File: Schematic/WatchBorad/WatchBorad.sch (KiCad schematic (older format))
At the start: 55 parts, among them IC1 TXS0108E, J1 Conn_01x06_Male, J10 Conn_01x07_Female, J2 Conn_01x09_Female, J3 USB_B_Mini, J4 Conn_01x10_Female, J5 Conn_01x06_Female, J6 Conn_01x04_Male, J7 Conn_01x11_Female, J8 Conn_01x11_Female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

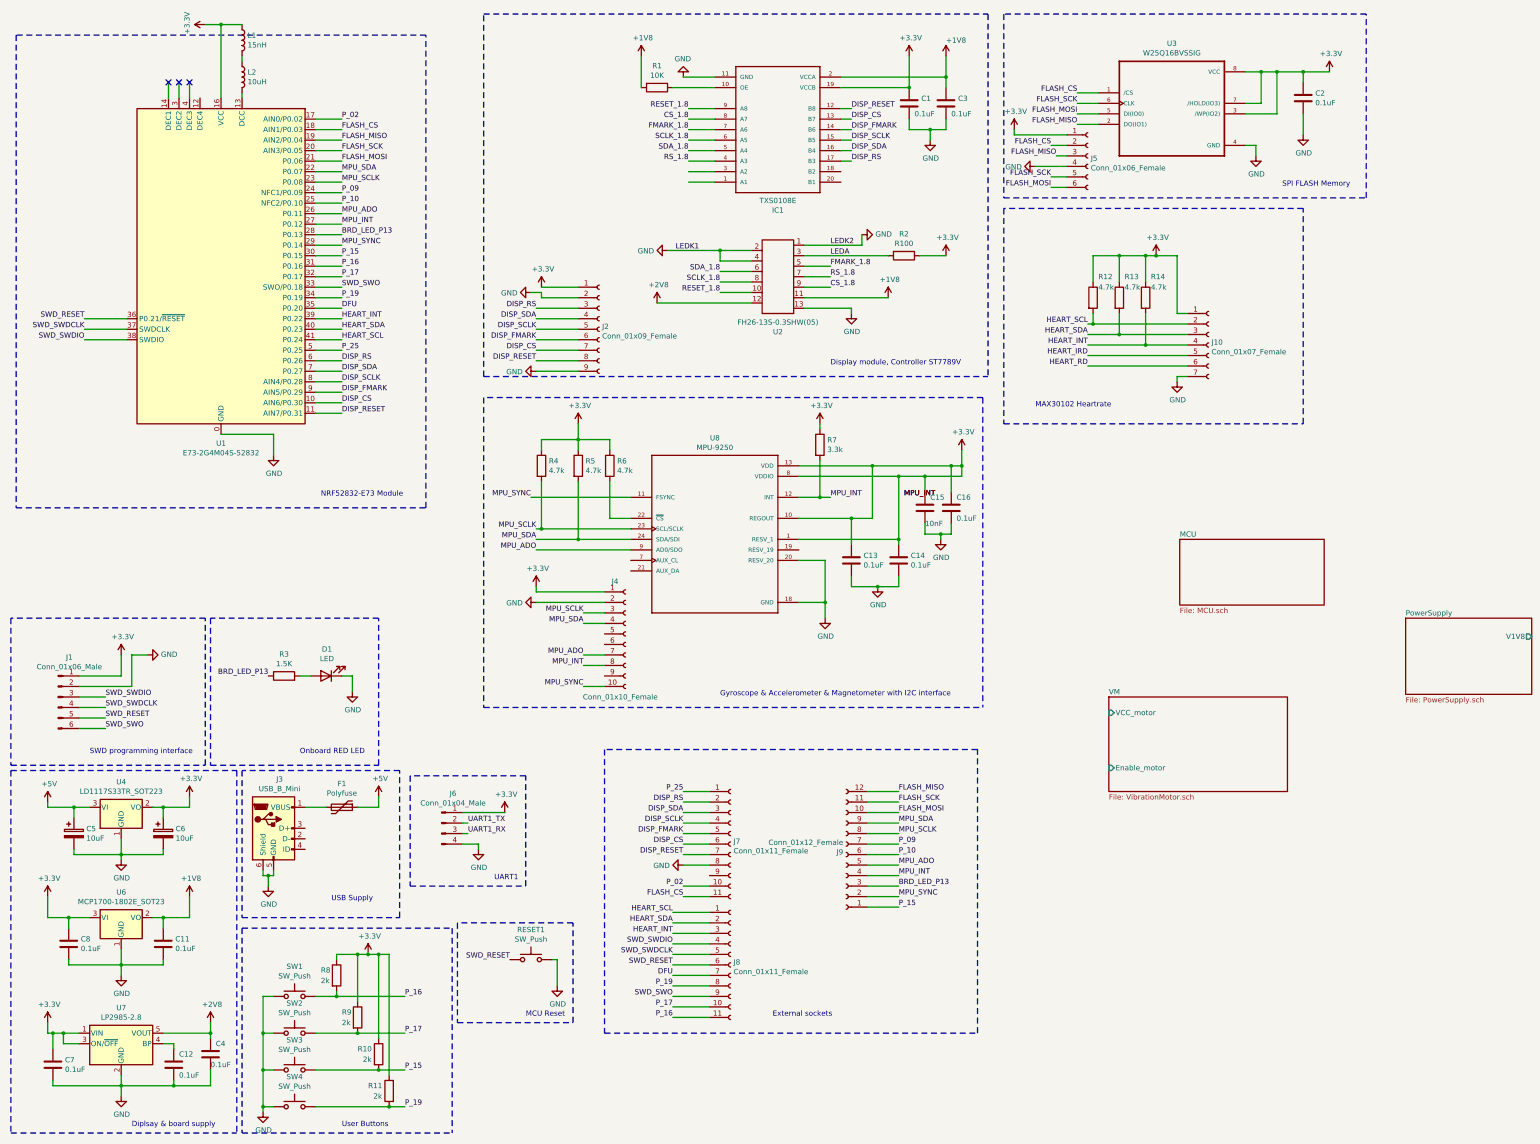
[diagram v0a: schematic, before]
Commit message: Added on/off circuit for PON and added other changes
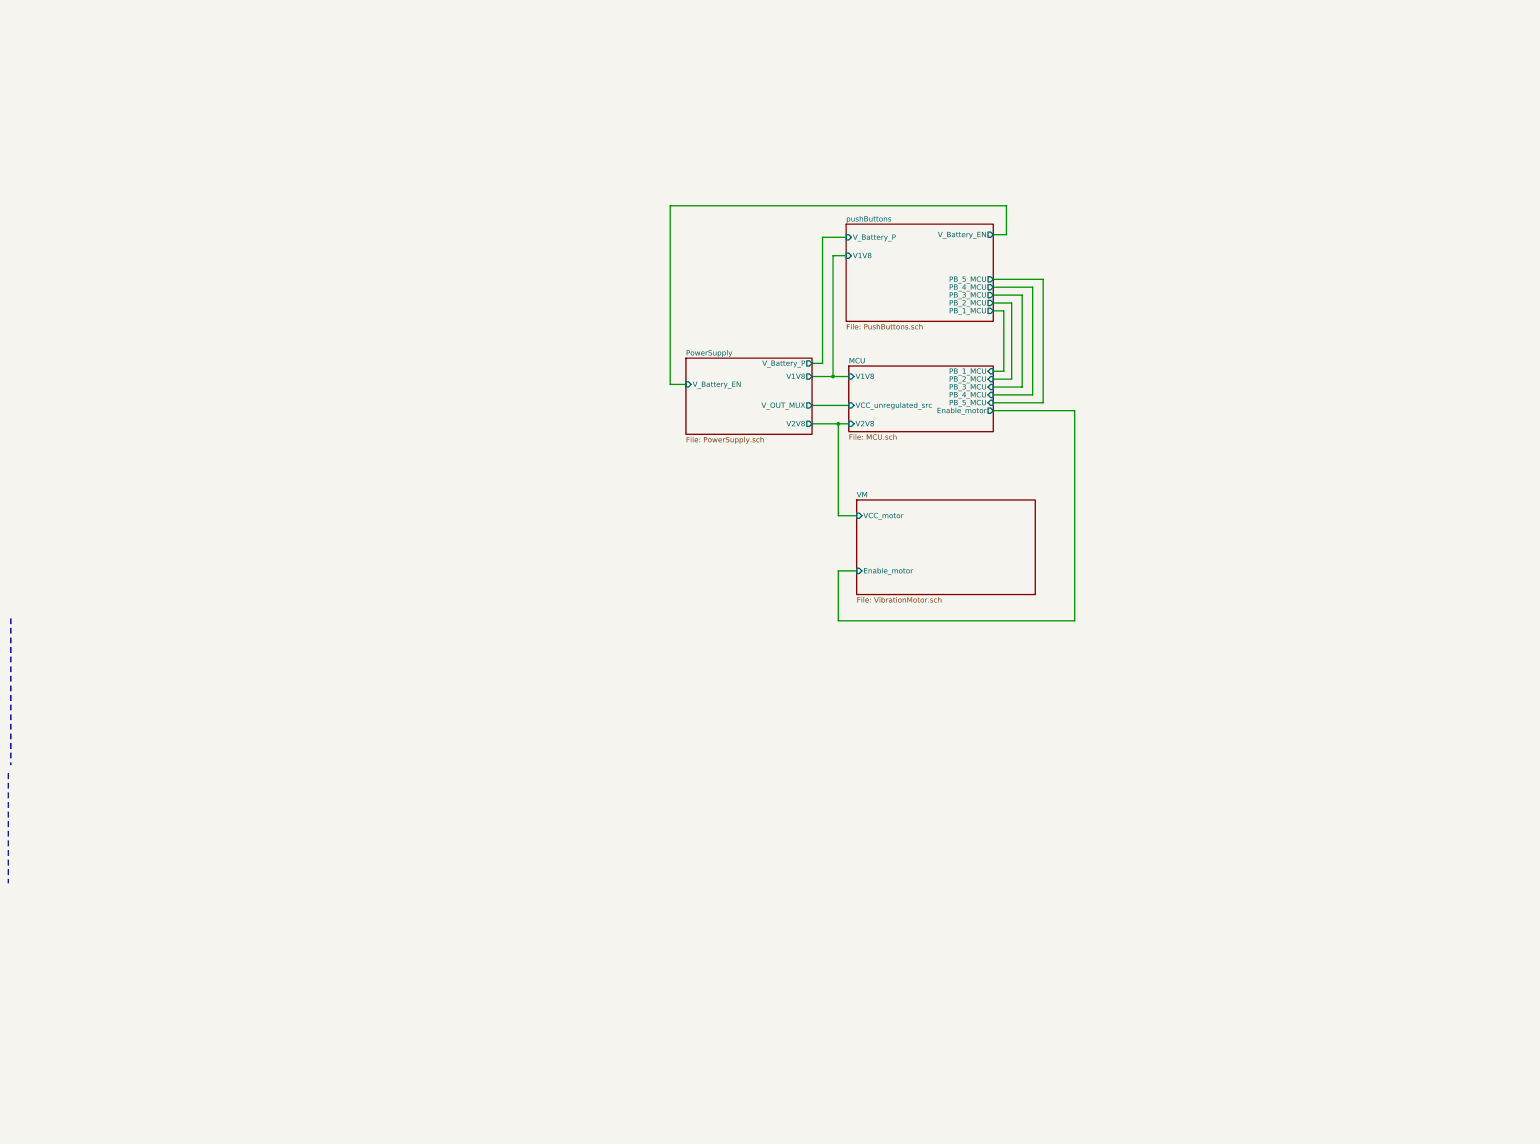
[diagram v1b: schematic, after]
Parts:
- removed C1, C11, C12, C13, C14, C16, C2, C3, C4, C7, C8: 0.1uF, Capacitor_SMD:C_0805_2012Metric_Pad1.15x1.40mm_HandSolder, symbol Device:C
- removed C15: 10nF, Capacitor_SMD:C_0805_2012Metric_Pad1.15x1.40mm_HandSolder, symbol Device:C
- removed C5, C6: 10uF, Capacitor_SMD:CP_Elec_4x3.9, symbol Device:CP
- removed D1: LED, LED_SMD:LED_0805_2012Metric_Pad1.15x1.40mm_HandSolder, symbol Device:LED
- removed F1: Polyfuse, Fuse:Fuse_1206_3216Metric_Pad1.42x1.75mm_HandSolder, symbol Device:Polyfuse
- removed IC1: TXS0108E, TXS0108E:PW_R-PDSO-G20, symbol WatchBorad-rescue:TXS0108E-TXS0108E
- removed J1: Conn_01x06_Male, Connector_PinHeader_2.54mm:PinHeader_1x06_P2.54mm_Vertical, symbol Connector:Conn_01x06_Male
- removed J10: Conn_01x07_Female, Connector_PinSocket_2.54mm:PinSocket_1x07_P2.54mm_Vertical, symbol Connector:Conn_01x07_Female
- removed J2: Conn_01x09_Female, Connector_PinSocket_2.54mm:PinSocket_1x09_P2.54mm_Vertical, symbol Connector:Conn_01x09_Female
- removed J3: USB_B_Mini, Connector_USB:USB_Mini-B_Lumberg_2486_01_Horizontal, symbol Connector:USB_B_Mini
- removed J4: Conn_01x10_Female, Connector_PinSocket_2.54mm:PinSocket_1x10_P2.54mm_Vertical, symbol Connector:Conn_01x10_Female
- removed J5: Conn_01x06_Female, Connector_PinSocket_2.54mm:PinSocket_1x06_P2.54mm_Vertical, symbol Connector:Conn_01x06_Female
- removed J6: Conn_01x04_Male, Connector_PinHeader_2.54mm:PinHeader_1x04_P2.54mm_Vertical, symbol Connector:Conn_01x04_Male
- removed J7, J8: Conn_01x11_Female, Connector_PinSocket_2.54mm:PinSocket_1x11_P2.54mm_Vertical, symbol Connector:Conn_01x11_Female
- removed J9: Conn_01x12_Female, Connector_PinSocket_2.54mm:PinSocket_1x12_P2.54mm_Vertical, symbol Connector:Conn_01x12_Female
- removed L1: 15nH, Inductor_SMD:L_0805_2012Metric_Pad1.15x1.40mm_HandSolder, symbol Device:L
- removed L2: 10uH, Inductor_SMD:L_0805_2012Metric_Pad1.15x1.40mm_HandSolder, symbol Device:L
- removed R1: 10K, Resistor_SMD:R_0805_2012Metric_Pad1.15x1.40mm_HandSolder, symbol Device:R
- removed R10, R11, R8, R9: 2k, Resistor_SMD:R_0805_2012Metric_Pad1.15x1.40mm_HandSolder, symbol Device:R
- removed R12, R13, R14: 4.7k, Resistor_SMD:R_0805_2012Metric, symbol Device:R
- removed R2: R100, Resistor_SMD:R_0805_2012Metric_Pad1.15x1.40mm_HandSolder, symbol Device:R
- removed R3: 1.5K, Resistor_SMD:R_0805_2012Metric_Pad1.15x1.40mm_HandSolder, symbol Device:R
- removed R4, R5, R6: 4.7k, Resistor_SMD:R_0805_2012Metric_Pad1.15x1.40mm_HandSolder, symbol Device:R
- removed R7: 3.3k, Resistor_SMD:R_0805_2012Metric_Pad1.15x1.40mm_HandSolder, symbol Device:R
- removed RESET1, SW1, SW2, SW3, SW4: SW_Push, Button_Switch_SMD:SW_SPST_SKQG_WithStem, symbol Switch:SW_Push
- removed U1: E73-2G4M04S-52832, RF_Module:E73-2G4M04S, symbol WatchBorad-rescue:E73-2G4M04S-52832-RF_Module
- removed U2: FH26-13S-0.3SHW(05), FH26W-13S-0:FH26-13S-0.3SHW(05), symbol WatchBorad-rescue:FH26-13S-0.3SHW(05)-Hirose_connectors
- removed U3: W25Q16BVSSIG, W25Q16BVSSIG:SOIC127P790X216-8N, symbol WatchBorad-rescue:W25Q16BVSSIG-W25Q16BVSSIG
- removed U4: LD1117S33TR_SOT223, Package_TO_SOT_SMD:SOT-223-3_TabPin2, symbol Regulator_Linear:LD1117S33TR_SOT223
- removed U6: MCP1700-1802E_SOT23, Package_TO_SOT_SMD:SOT-23, symbol Regulator_Linear:MCP1700-1802E_SOT23
- removed U7: LP2985-2.8, Package_TO_SOT_SMD:SOT-23-5, symbol Regulator_Linear:LP2985-2.8
- removed U8: MPU-9250, QFN40P300X300X105-24N, symbol WatchBorad-rescue:MPU-9250-MPU-9250
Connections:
- no-connect marks 3 -> 0
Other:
- note removed: "Diplsay & board supply"
- note removed: "Display module, Controller ST7789V"
- note removed: "External sockets"
- note removed: "Gyroscope & Accelerometer & Magnetometer with I2C interface"
- note removed: "MAX30102 Heartrate"
- note removed: "MCU Reset"
- note removed: "NRF52832-E73 Module"
- note removed: "Onboard RED LED"
- note removed: "SPI FLASH Memory\n"
- note removed: "SWD programming interface"
- note removed: "UART1"
- note removed: "USB Supply"
- note removed: "User Buttons"

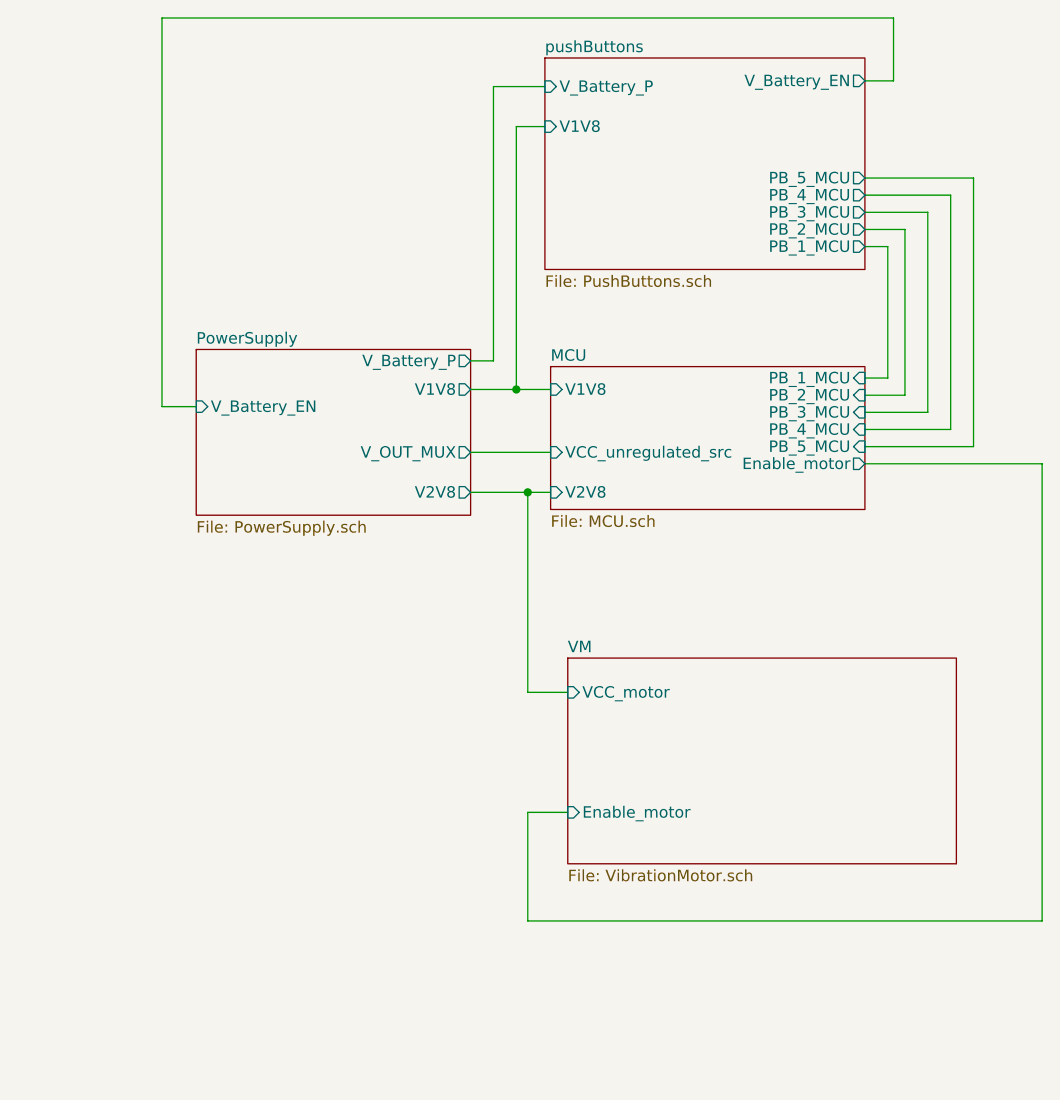
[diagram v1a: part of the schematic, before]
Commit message: Display is replaced, now it has single power supply. One PSU is removed. Circuit PB is modified.
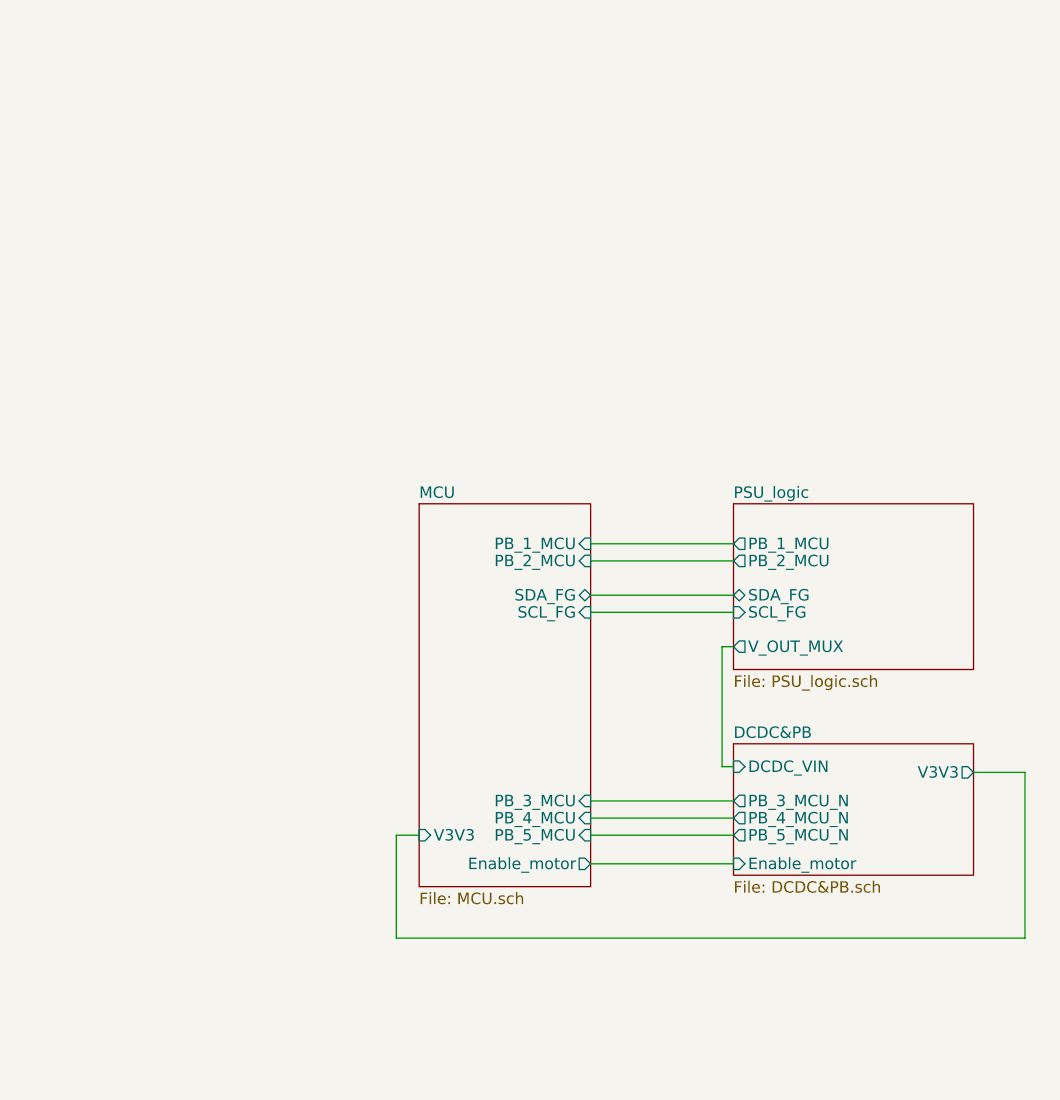
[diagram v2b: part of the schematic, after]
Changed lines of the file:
@@
 $Descr A3 16535 11693
 encoding utf-8
-Sheet 1 5
+Sheet 1 4
 Title ""
 Date ""
@@
 	575  7775 575  8825
 $Sheet
-S 8650 5175 1700 900
-U 5EA4867C
-F0 "VM" 50
-F1 "VibrationMotor.sch" 50
-F2 "VCC_motor" I L 8650 5325 50
-F3 "Enable_motor" I L 8650 5850 50
-$EndSheet
-$Sheet
-S 8575 3900 1375 625
+S 8000 4500 750  1675
 U 5E9B1DCE
 F0 "MCU" 50
 F1 "MCU.sch" 50
-F2 "VCC_unregulated_src" I L 8575 4275 50
-F3 "PB_1_MCU" I R 9950 3950 50
-F4 "PB_2_MCU" I R 9950 4025 50
-F5 "PB_3_MCU" I R 9950 4100 50
-F6 "PB_4_MCU" I R 9950 4175 50
-F7 "PB_5_MCU" I R 9950 4250 50
-F8 "V1V8" I L 8575 4000 50
-F9 "V2V8" I L 8575 4450 50
-F10 "Enable_motor" O R 9950 4325 50
+F2 "PB_1_MCU" I R 8750 4675 50
+F3 "PB_2_MCU" I R 8750 4750 50
+F4 "PB_3_MCU" I R 8750 5800 50
+F5 "PB_4_MCU" I R 8750 5875 50
+F6 "PB_5_MCU" I R 8750 5950 50
+F7 "Enable_motor" O R 8750 6075 50
+F8 "V3V3" I L 8000 5950 50
+F9 "SDA_FG" B R 8750 4900 50
+F10 "SCL_FG" I R 8750 4975 50
+$EndSheet
+$Sheet
+S 9375 4500 1050 725
+U 5F913559
+F0 "PSU_logic" 50
+F1 "PSU_logic.sch" 50
+F2 "PB_1_MCU" O L 9375 4675 50
+F3 "PB_2_MCU" O L 9375 4750 50
+F4 "V_OUT_MUX" O L 9375 5125 50
+F5 "SDA_FG" B L 9375 4900 50
+F6 "SCL_FG" I L 9375 4975 50
+$EndSheet
+$Sheet
+S 9375 5550 1050 575
+U 5F988DA5
+F0 "DCDC&PB" 50
+F1 "DCDC&PB.sch" 50
+F2 "V3V3" O R 10425 5675 50
+F3 "PB_3_MCU_N" O L 9375 5800 50
+F4 "PB_4_MCU_N" O L 9375 5875 50
+F5 "PB_5_MCU_N" O L 9375 5950 50
+F6 "Enable_motor" I L 9375 6075 50
+F7 "DCDC_VIN" I L 9375 5650 50
 $EndSheet
 Wire Wire Line
-	8225 4275 8575 4275
+	9375 5125 9325 5125
 Wire Wire Line
-	8225 4450 8475 4450
+	9325 5125 9325 5650
 Wire Wire Line
-	8475 4450 8475 5325
+	9325 5650 9375 5650
 Wire Wire Line
-	8475 5325 8650 5325
-$Sheet
-S 8550 2550 1400 925
-U 5ED3F98E
-F0 "pushButtons" 50
-F1 "PushButtons.sch" 50
-F2 "V_Battery_P" I L 8550 2675 50
-F3 "V_Battery_EN" O R 9950 2650 50
-F4 "PB_2_MCU" O R 9950 3300 50
-F5 "V1V8" I L 8550 2850 50
-F6 "PB_3_MCU" O R 9950 3225 50
-F7 "PB_4_MCU" O R 9950 3150 50
-F8 "PB_5_MCU" O R 9950 3075 50
-F9 "PB_1_MCU" O R 9950 3375 50
-$EndSheet
-$Sheet
-S 7025 3825 1200 725
-U 5E9C1C3A
-F0 "PowerSupply" 50
-F1 "PowerSupply.sch" 50
-F2 "V1V8" O R 8225 4000 50
-F3 "V_OUT_MUX" O R 8225 4275 50
-F4 "V2V8" O R 8225 4450 50
-F5 "V_Battery_P" O R 8225 3875 50
-F6 "V_Battery_EN" I L 7025 4075 50
-$EndSheet
+	8000 5950 7900 5950
 Wire Wire Line
-	8225 3875 8325 3875
+	7900 5950 7900 6400
 Wire Wire Line
-	8550 2675 8325 2675
+	7900 6400 10650 6400
 Wire Wire Line
-	8325 2675 8325 3875
+	10650 6400 10650 5675
 Wire Wire Line
-	8550 2850 8425 2850
+	10650 5675 10425 5675
 Wire Wire Line
-	8425 2850 8425 4000
+	8750 5950 9375 5950
 Wire Wire Line
-	8425 4000 8225 4000
+	8750 5875 9375 5875
 Wire Wire Line
-	9950 2650 10075 2650
+	8750 6075 9375 6075
 Wire Wire Line
-	10075 2650 10075 2375
+	8750 5800 9375 5800
 Wire Wire Line
-	10075 2375 6875 2375
+	8750 4675 9375 4675
 Wire Wire Line
-	6875 2375 6875 4075
+	9375 4750 8750 4750
 Wire Wire Line
-	6875 4075 7025 4075
+	8750 4975 9375 4975
 Wire Wire Line
-	9950 3375 10050 3375
-Wire Wire Line
-	10050 3375 10050 3950
-Wire Wire Line
-	9950 3950 10050 3950
-Wire Wire Line
-	9950 3300 10125 3300
-Wire Wire Line
-	10125 3300 10125 4025
-Wire Wire Line
-	10125 4025 9950 4025
-Wire Wire Line
-	9950 3225 10225 3225
-Wire Wire Line
-	10225 3225 10225 4100
-Wire Wire Line
-	10225 4100 9950 4100
-Wire Wire Line
-	9950 3150 10325 3150
-Wire Wire Line
-	10325 3150 10325 4175
-Wire Wire Line
-	10325 4175 9950 4175
-Wire Wire Line
-	9950 3075 10425 3075
-Wire Wire Line
-	10425 3075 10425 4250
-Wire Wire Line
-	10425 4250 9950 4250
-Connection ~ 8475 4450
-Wire Wire Line
-	8475 4450 8575 4450
-Wire Wire Line
-	8575 4000 8425 4000
-Connection ~ 8425 4000
-Wire Wire Line
-	9950 4325 10725 4325
-Wire Wire Line
-	10725 4325 10725 6325
-Wire Wire Line
-	10725 6325 8475 6325
-Wire Wire Line
-	8475 6325 8475 5850
-Wire Wire Line
-	8475 5850 8650 5850
+	9375 4900 8750 4900
 $EndSCHEMATC

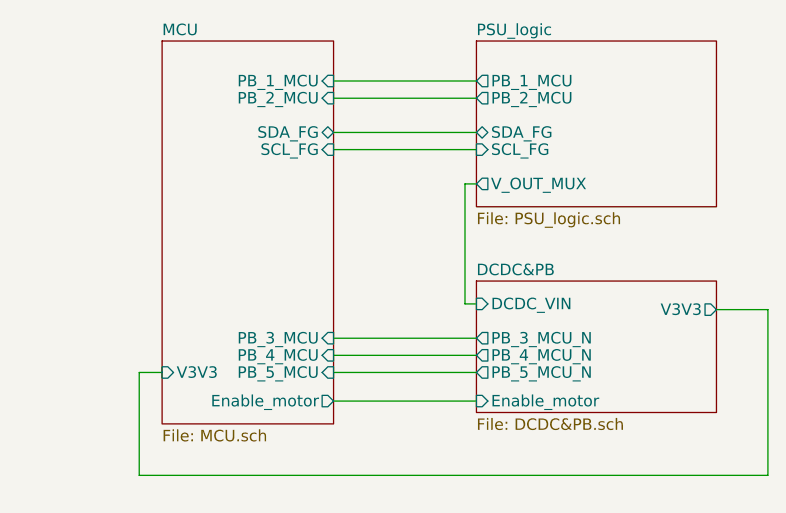
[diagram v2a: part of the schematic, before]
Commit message: Updated & fixed missed SCH parts list
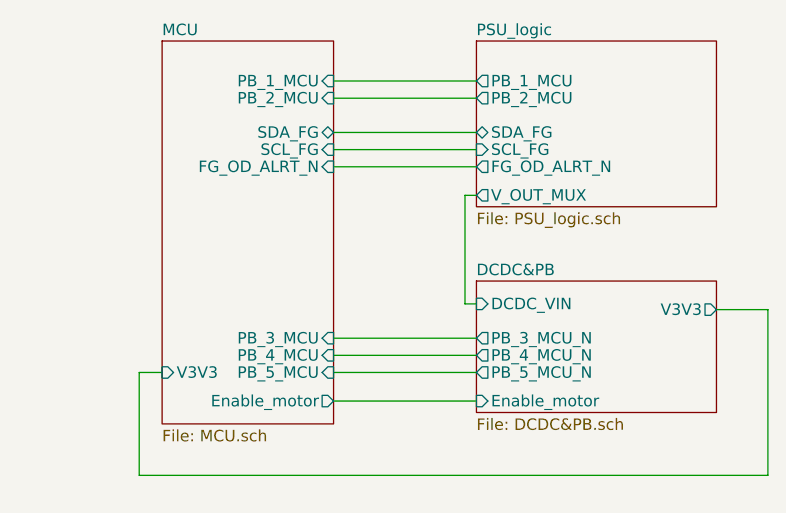
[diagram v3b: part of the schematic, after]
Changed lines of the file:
@@
 F9 "SDA_FG" B R 8750 4900 50
 F10 "SCL_FG" I R 8750 4975 50
+F11 "FG_OD_ALRT_N" I R 8750 5050 50
 $EndSheet
 $Sheet
@@
 F2 "PB_1_MCU" O L 9375 4675 50
 F3 "PB_2_MCU" O L 9375 4750 50
-F4 "V_OUT_MUX" O L 9375 5125 50
+F4 "V_OUT_MUX" O L 9375 5175 50
 F5 "SDA_FG" B L 9375 4900 50
 F6 "SCL_FG" I L 9375 4975 50
+F7 "FG_OD_ALRT_N" O L 9375 5050 50
 $EndSheet
 $Sheet
@@
 $EndSheet
 Wire Wire Line
-	9375 5125 9325 5125
+	9375 5175 9325 5175
 Wire Wire Line
-	9325 5125 9325 5650
+	9325 5175 9325 5650
 Wire Wire Line
 	9325 5650 9375 5650
@@
 Wire Wire Line
 	9375 4900 8750 4900
+Wire Wire Line
+	8750 5050 9375 5050
 $EndSCHEMATC
